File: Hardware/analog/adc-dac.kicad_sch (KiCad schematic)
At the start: 11 parts

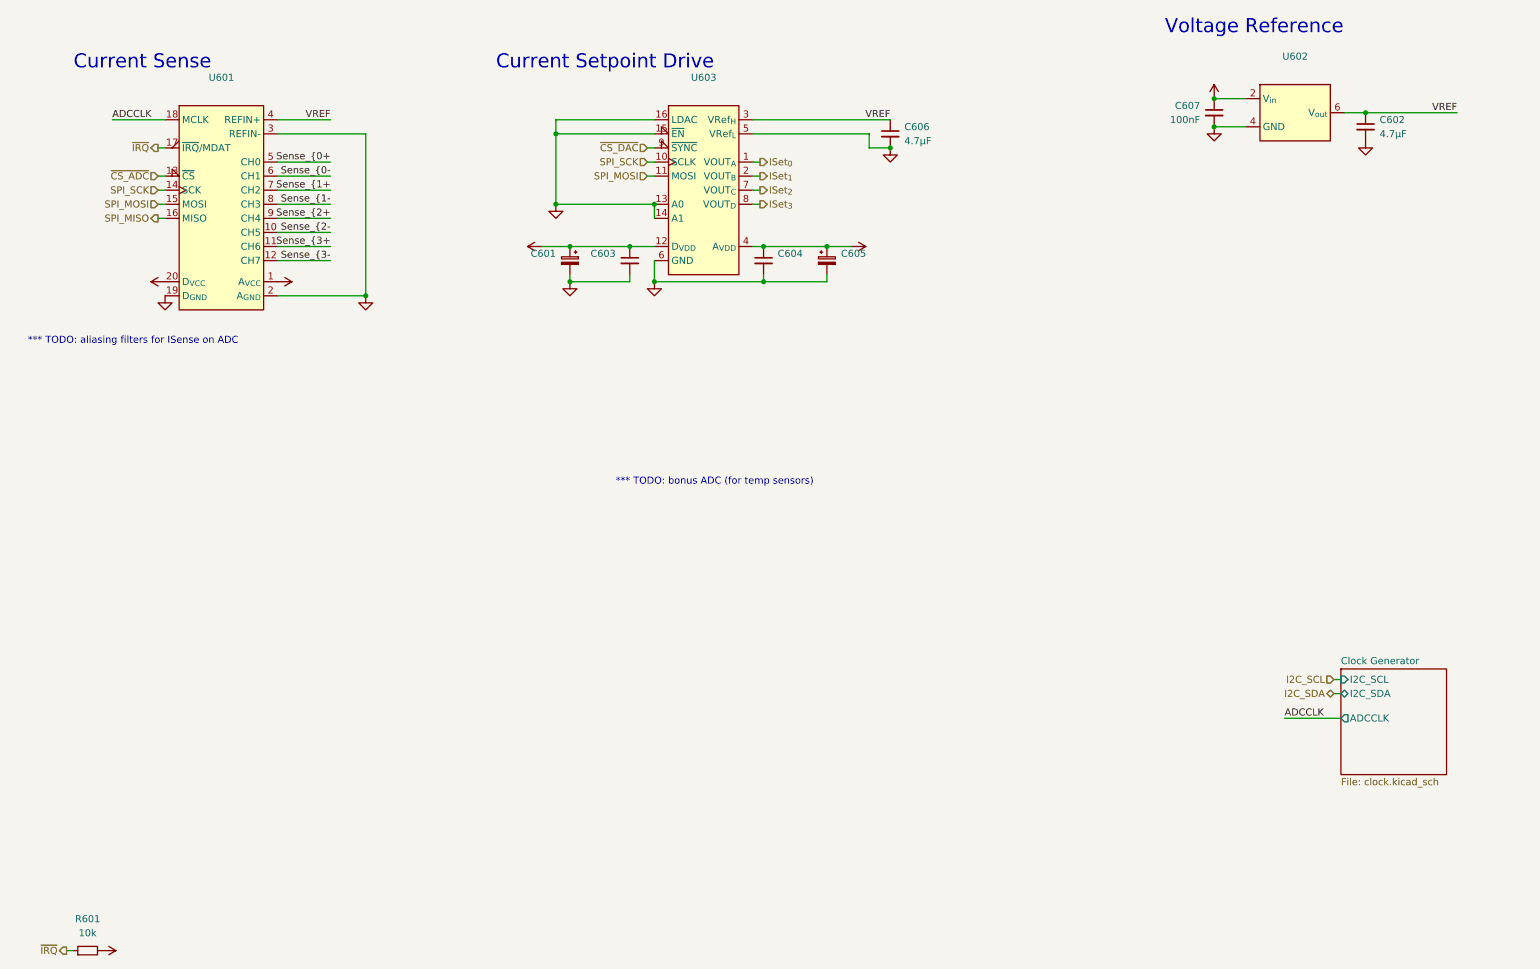
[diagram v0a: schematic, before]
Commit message: Add ADC aliasing filters
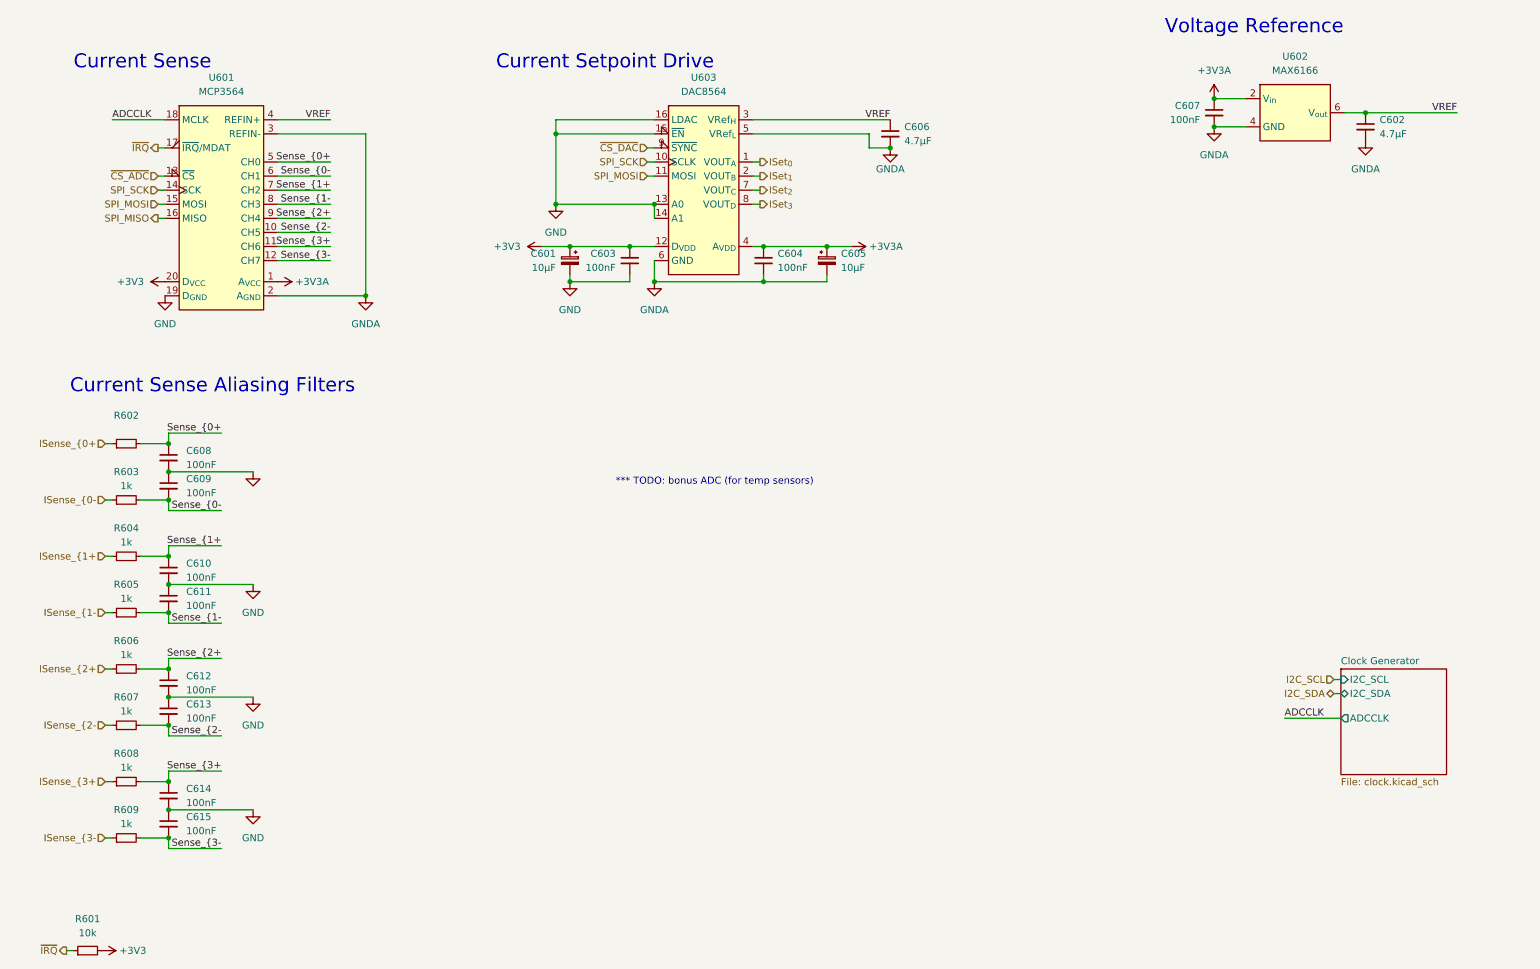
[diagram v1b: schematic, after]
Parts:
- added C608, C609, C610, C611, C612, C613, C614, C615: 100nF, Capacitor_SMD:C_0805_2012Metric_Pad1.18x1.45mm_HandSolder, symbol Device:C_Small
- added R602: (no value), symbol Device:R_Small
- added R603, R604, R605, R606, R607, R608, R609: 1k, Resistor_SMD:R_0805_2012Metric_Pad1.20x1.40mm_HandSolder, symbol Device:R_Small
- C601, C605: value (none) -> 10µF; footprint (none) -> Capacitor_Tantalum_SMD:CP_EIA-3216-18_Kemet-A_Pad1.58x1.35mm_HandSolder
- C603, C604: value (none) -> 100nF; footprint (none) -> Capacitor_SMD:C_0805_2012Metric_Pad1.18x1.45mm_HandSolder
- U601: value (none) -> MCP3564; footprint (none) -> Package_SO:TSSOP-20_4.4x6.5mm_P0.65mm
- U602: value (none) -> MAX6166; footprint (none) -> Package_SO:SOIC-8_3.9x4.9mm_P1.27mm
- U603: value (none) -> DAC8564
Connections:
- net GND: now also C608.2, C609.1, C610.2, C611.1, C612.2, C613.1, C614.2, C615.1
- net Sense_{0+: now also C608.1, R602.2
- net Sense_{0-: now also C609.2, R603.2
- net Sense_{1+: now also C610.1, R604.2
- net Sense_{1-: now also C611.2, R605.2
- net Sense_{2+: now also C612.1, R606.2
- net Sense_{2-: now also C613.2, R607.2
- net Sense_{3+: now also C614.1, R608.2
- net Sense_{3-: now also C615.2, R609.2
- new net ISense_{0+: R602.1
- new net ISense_{0-: R603.1
- new net ISense_{1+: R604.1
- new net ISense_{1-: R605.1
- new net ISense_{2+: R606.1
- new net ISense_{2-: R607.1
- new net ISense_{3+: R608.1
- new net ISense_{3-: R609.1
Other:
- note added: "Current Sense Aliasing Filters"
- note removed: "*** TODO: aliasing filters for ISense on ADC"

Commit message: Work on layout analog board
- Moved the heatsink to be horizontal near the bottom of the analog
  board, to give more open space for the analog circuitry away from the
  hot MOSFETs

- Minor tweak to bonus display (cutout for front panel jacks)
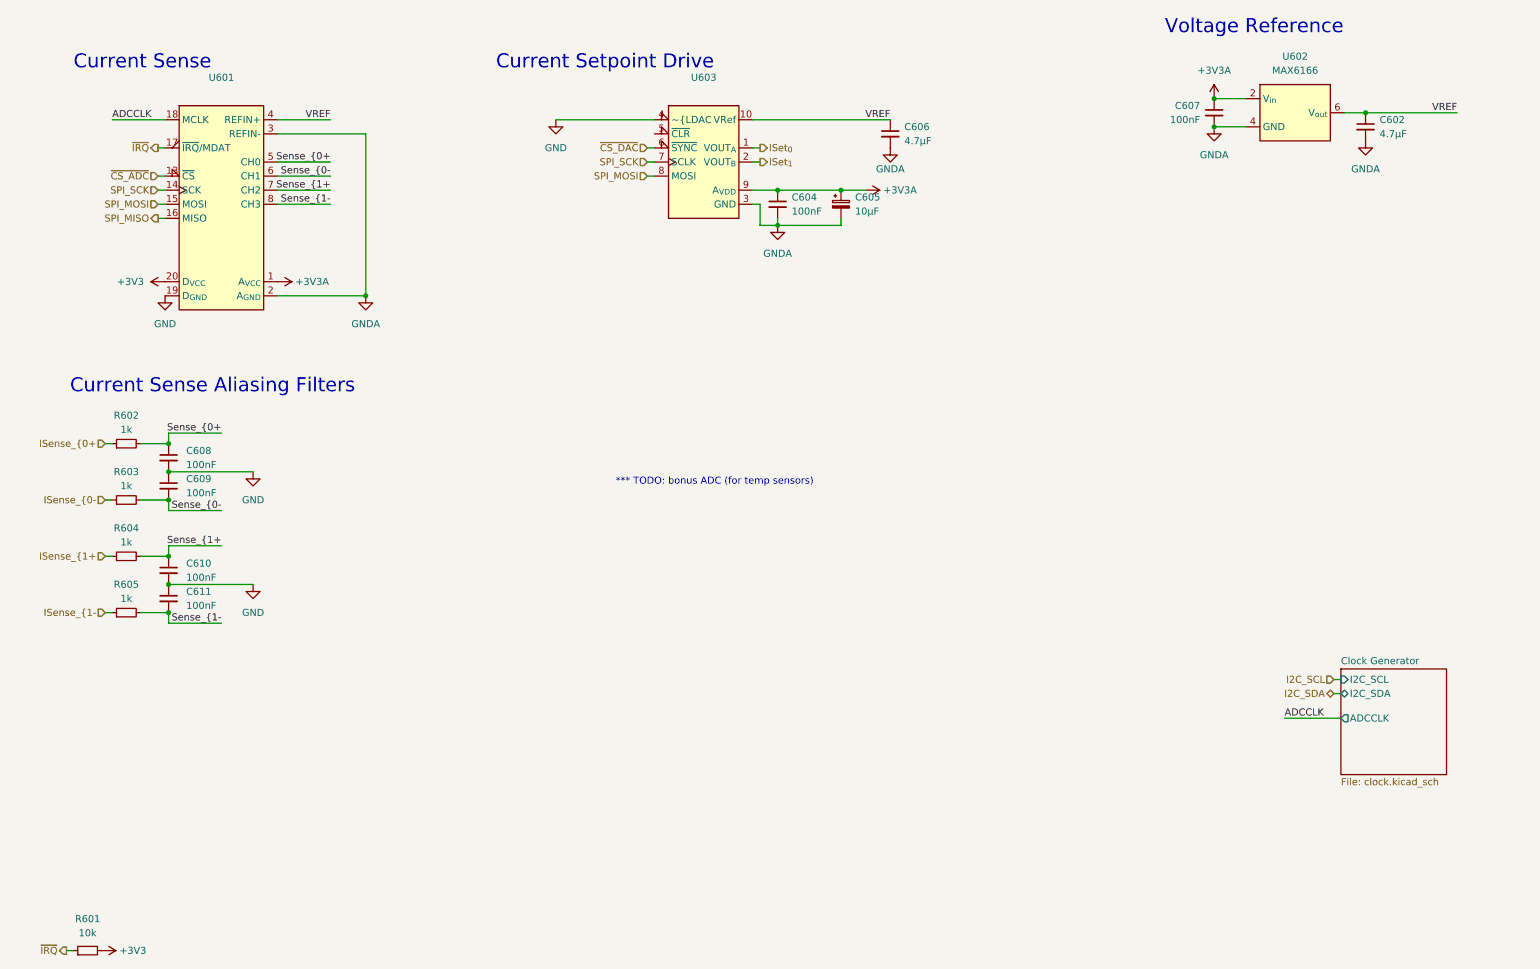
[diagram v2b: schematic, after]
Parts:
- removed C601: 10µF, Capacitor_Tantalum_SMD:CP_EIA-3216-18_Kemet-A_Pad1.58x1.35mm_HandSolder, symbol Device:C_Polarized_Small
- removed C603, C612, C613, C614, C615: 100nF, Capacitor_SMD:C_0805_2012Metric_Pad1.18x1.45mm_HandSolder, symbol Device:C_Small
- removed R606, R607, R608, R609: 1k, Resistor_SMD:R_0805_2012Metric_Pad1.20x1.40mm_HandSolder, symbol Device:R_Small
- removed U603: DAC8564, Package_SO:TSSOP-16_4.4x5mm_P0.65mm, symbol programmable-load:DAC8564
- added U603: (no value), symbol programmable-load:DAC8562
- R602: value (none) -> 1k; footprint (none) -> Resistor_SMD:R_0805_2012Metric_Pad1.20x1.40mm_HandSolder
- U601: value MCP3564 -> (none); footprint Package_SO:TSSOP-20_4.4x6.5mm_P0.65mm -> (none); symbol programmable-load:MCP3564 -> programmable-load:MCP3562
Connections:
- net +3V3A: now also U603.9 (A_{VDD})
- net GND: now also U603.4 (~{LDAC)
- net GNDA: now also U603.3 (GND)
- net ISet_{0}: now also U603.1 (VOUT_{A})
- net ISet_{1}: now also U603.2 (VOUT_{B})
- net SPI_MOSI: now also U603.8 (MOSI)
- net SPI_SCK: now also U603.7 (SCLK)
- net VREF: now also U603.10 (VRef)
- net ~{CS_DAC}: now also U603.6 (~{SYNC})
- net Sense_{2+: no longer names the net of U601.9 (CH4)
- net Sense_{2-: no longer names the net of U601.10 (CH5)
- net Sense_{3+: no longer names the net of U601.11 (CH6)
- net Sense_{3-: no longer names the net of U601.12 (CH7)
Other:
- moved on the sheet: C604, C605

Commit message: Start work on analog island
- This is the part with the ADC/DAC/reference which has its own analog
  ground and voltage, generated from +5V
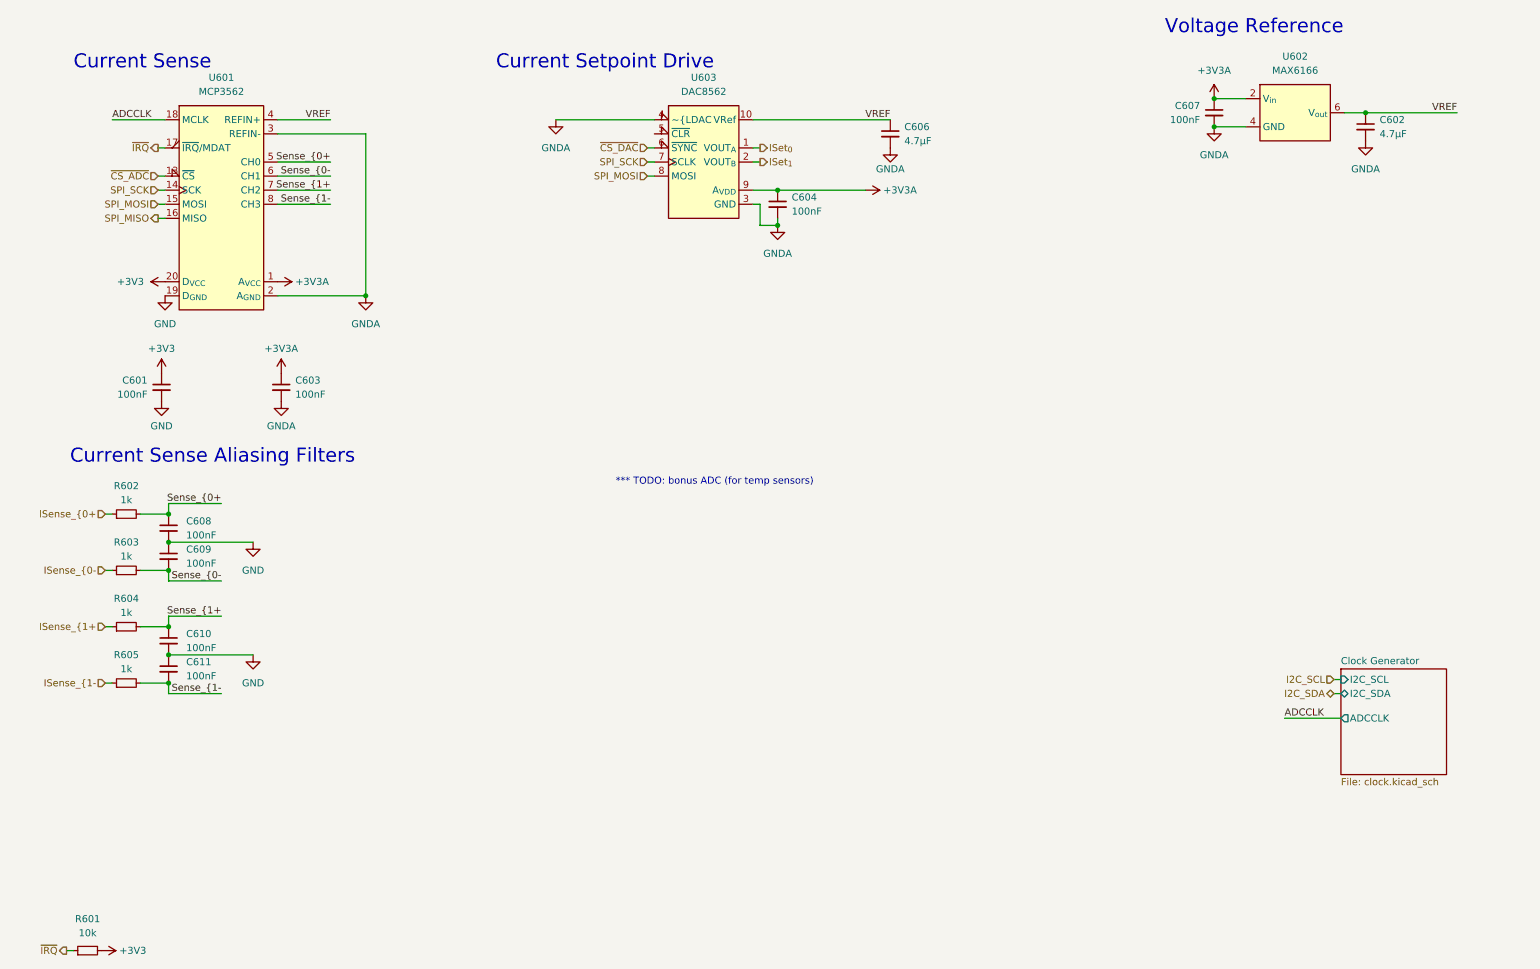
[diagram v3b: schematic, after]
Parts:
- removed C605: 10µF, Capacitor_Tantalum_SMD:CP_EIA-3216-18_Kemet-A_Pad1.58x1.35mm_HandSolder, symbol Device:C_Polarized_Small
- added C601, C603: 100nF, Capacitor_SMD:C_0805_2012Metric_Pad1.18x1.45mm_HandSolder, symbol Device:C_Small
- U601: value (none) -> MCP3562; footprint (none) -> Package_SO:TSSOP-20_4.4x6.5mm_P0.65mm
- U603: value (none) -> DAC8562; footprint (none) -> Package_SO:MSOP-10_3x3mm_P0.5mm
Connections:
- net +3V3: now also C601.1
- net +3V3A: now also C603.1
- net GND: now also C601.2; no longer U603.4 (~{LDAC)
- net GNDA: now also U603.4 (~{LDAC), C603.2
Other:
- moved on the sheet: C608, C609, C610, C611, R602, R603, R604, R605

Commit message: Initial pass at analog board
- Everything currently in the schematic is routed, and stuff is
  reasonably sanely laid out

- Some compromises: namely, the zero offset doesn't use the DAC
  reference for its positive, but generates a separate 2.5V via the
  shunt diodes; this is then shared between both op-amps. That avoids
  the DAC/ADC reference getting noisified

  Also, we don't have an ADC for measuring the temperature sensors yet,
  and in fact, those aren't routed out (or existent really) yet either

- TODO: add test points for drive voltages and current sense voltages
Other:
- title: (none) -> 300W Analog Load Board
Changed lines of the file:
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@@
 (kicad_sch (version 20211123) (generator eeschema)
   (paper "A4")
+  (title_block
+    (title "300W Analog Load Board")
+    (rev "1")
+  )
   (junction (at 42.545 130.81) (diameter 0) (color 0 0 0 0)
   )
